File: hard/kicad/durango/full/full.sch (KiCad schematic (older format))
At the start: 38 parts, among them J1 NANOLINK, J2 IOX8, J3 BIOX9, J4 BUZZER, Q1 BC547, Q2 BC547, Q3 BC547, SW1 RESET, U1 65C02, U104 74HC257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

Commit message: adapting references to breadboard
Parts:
- U19: value 74HC00* -> 74HC00
- U20: value 74HC74* -> 74HC74
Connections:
- net A0: now also U20.12 (D); no longer U20.2 (D)
- net D0: now also U20.2 (D); no longer U20.12 (D)
- net GND: now also U28.1; no longer U28.2
- net IEN: now also U20.9 (Q); no longer U20.5 (Q)
- net ~DWE: now also U28.8; no longer U28.11
- net ~IEN: now also U20.8 (~Q); no longer U20.6 (~Q)
- net ~IOAQ: now also U20.11 (C); no longer U20.3 (C)
- net ~IOBQ: now also U20.3 (C); no longer U20.11 (C)
- net ~WE: now also U28.2, U28.9; no longer U28.1, U28.13
- net ~WE2: now also U28.12, U28.13; no longer U28.10, U28.9
- net ~WE3: now also U28.10, U28.11; no longer U28.12, U28.8
- net at D2.2 (A): now also U20.5 (Q); no longer U20.9 (Q)
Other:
- moved on the sheet: U20A, U20B, U28C, U28D
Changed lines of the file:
@@
 EESchema Schematic File Version 4
 LIBS:full-cache
-EELAYER 29 0
+EELAYER 30 0
 EELAYER END
 $Descr A4 11693 8268
@@
 P 3450 4200
 F 0 "U19" V 3404 4020 50  0000 R CNN
-F 1 "74HC00*" V 3495 4020 50  0000 R CNN
+F 1 "74HC00" V 3495 4020 50  0000 R CNN
 F 2 "Package_DIP:DIP-14_W7.62mm" H 3450 4200 50  0001 C CNN
 F 3 "http://www.ti.com/lit/gpn/sn74hct00" H 3450 4200 50  0001 C CNN
@@
 P 3750 4700
 F 0 "U19" H 3400 4500 50  0000 L CNN
-F 1 "74HC00*" H 3650 4500 50  0000 L CNN
+F 1 "74HC00" H 3650 4500 50  0000 L CNN
 F 2 "Package_DIP:DIP-14_W7.62mm" H 3750 4700 50  0001 C CNN
 F 3 "http://www.ti.com/lit/gpn/sn74hct00" H 3750 4700 50  0001 C CNN
@@
 L 74xx:74HC74 U20
 U 1 1 61846FEF
+P 9400 5800
+F 0 "U20" H 9400 6281 50  0000 C CNN
+F 1 "74HC74" H 9400 6190 50  0000 C CNN
+F 2 "Package_DIP:DIP-14_W7.62mm" H 9400 5800 50  0001 C CNN
+F 3 "74xx/74hc_hct74.pdf" H 9400 5800 50  0001 C CNN
+	1    9400 5800
+	1    0    0    -1
+$EndComp
+$Comp
+L 74xx:74HC74 U20
+U 2 1 6184A5B7
 P 8400 5800
 F 0 "U20" H 8400 6281 50  0000 C CNN
-F 1 "74HC74*" H 8400 6190 50  0000 C CNN
+F 1 "74HC74" H 8400 6190 50  0000 C CNN
 F 2 "Package_DIP:DIP-14_W7.62mm" H 8400 5800 50  0001 C CNN
 F 3 "74xx/74hc_hct74.pdf" H 8400 5800 50  0001 C CNN
-	1    8400 5800
-	1    0    0    -1
-$EndComp
-$Comp
-L 74xx:74HC74 U20
-U 2 1 6184A5B7
-P 9400 5800
-F 0 "U20" H 9400 6281 50  0000 C CNN
-F 1 "74HC74*" H 9400 6190 50  0000 C CNN
-F 2 "Package_DIP:DIP-14_W7.62mm" H 9400 5800 50  0001 C CNN
-F 3 "74xx/74hc_hct74.pdf" H 9400 5800 50  0001 C CNN
-	2    9400 5800
+	2    8400 5800
 	1    0    0    -1
 $EndComp
@@
 Wire Wire Line
 	9100 5800 9100 6400
-Wire Wire Line
-	9100 6400 7200 6400
 Text Label 9100 5700 2    50   ~ 0
 D0
@@
 U 1 1 60967ED5
 P 10500 4500
-F 0 "U28" V 10454 4688 50  0000 L CNN
-F 1 "74HC32" V 10545 4688 50  0000 L CNN
+F 0 "U28" V 10350 4100 50  0000 L CNN
+F 1 "74HC32" V 10450 4050 50  0000 L CNN
 F 2 "Package_DIP:DIP-14_W7.62mm" H 10500 4500 50  0001 C CNN
 F 3 "http://www.ti.com/lit/gpn/sn74LS32" H 10500 4500 50  0001 C CNN
 	1    10500 4500
-	0    -1   1    0
+	0    1    1    0
 $EndComp
 $Comp
@@
 L 74xx:74LS32 U28
 U 3 1 6096C7E5
+P 9400 3900
+F 0 "U28" V 9450 4300 50  0000 R CNN
+F 1 "74HC32" V 9350 4400 50  0000 R CNN
+F 2 "Package_DIP:DIP-14_W7.62mm" H 9400 3900 50  0001 C CNN
+F 3 "http://www.ti.com/lit/gpn/sn74LS32" H 9400 3900 50  0001 C CNN
+	3    9400 3900
+	0    1    -1   0
+$EndComp
+$Comp
+L 74xx:74LS32 U28
+U 4 1 6096F4C6
 P 9600 4800
-F 0 "U28" H 9650 5000 50  0000 R CNN
-F 1 "74HC32" H 9700 4600 50  0000 R CNN
+F 0 "U28" H 9700 4500 50  0000 R CNN
+F 1 "74HC32" H 9750 4600 50  0000 R CNN
 F 2 "Package_DIP:DIP-14_W7.62mm" H 9600 4800 50  0001 C CNN
 F 3 "http://www.ti.com/lit/gpn/sn74LS32" H 9600 4800 50  0001 C CNN
-	3    9600 4800
-	-1   0    0    -1
-$EndComp
-$Comp
-L 74xx:74LS32 U28
-U 4 1 6096F4C6
-P 9400 3900
-F 0 "U28" V 9446 3720 50  0000 R CNN
-F 1 "74HC32" V 9355 3720 50  0000 R CNN
-F 2 "Package_DIP:DIP-14_W7.62mm" H 9400 3900 50  0001 C CNN
-F 3 "http://www.ti.com/lit/gpn/sn74LS32" H 9400 3900 50  0001 C CNN
-	4    9400 3900
-	0    -1   -1   0
+	4    9600 4800
+	-1   0    0    1
 $EndComp
 Wire Wire Line
@@
 Wire Wire Line
 	9900 4700 9900 4900
-Connection ~ 9900 4900
 Wire Wire Line
 	10400 4200 9500 4200
@@
 ~RESET
 Wire Wire Line
+	7200 6400 9100 6400
+Wire Wire Line
 	2550 6200 3000 6200
 Wire Wire Line
@@
 	5850 950  5850 5100
 Wire Bus Line
+	10800 650  10800 1650
+Wire Bus Line
 	7450 950  7450 5050
 Wire Bus Line
-	10800 650  10800 1650
-Wire Bus Line
 	1650 5800 1650 6900
 Wire Bus Line
@@
 Wire Bus Line
 	4250 700  4250 6450
+Connection ~ 9900 4900
 $EndSCHEMATC

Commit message: fixed 74HC00 notation
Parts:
- U19: value 74HC00* -> 74HC00
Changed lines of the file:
@@
 EESchema Schematic File Version 4
 LIBS:full-cache
-EELAYER 30 0
+EELAYER 29 0
 EELAYER END
 $Descr A4 11693 8268
@@
 P 3800 5900
 F 0 "U19" V 3900 6300 50  0000 R CNN
-F 1 "74HC00*" V 3700 6450 50  0000 R CNN
+F 1 "74HC00" V 3700 6450 50  0000 R CNN
 F 2 "Package_DIP:DIP-14_W7.62mm" H 3800 5900 50  0001 C CNN
 F 3 "http://www.ti.com/lit/gpn/sn74hct00" H 3800 5900 50  0001 C CNN
@@
 Wire Wire Line
 	7200 6400 9100 6400
+Connection ~ 9900 4900
 Wire Wire Line
 	2550 6200 3000 6200
@@
 	5850 950  5850 5100
 Wire Bus Line
+	7450 950  7450 5050
+Wire Bus Line
 	10800 650  10800 1650
 Wire Bus Line
-	7450 950  7450 5050
-Wire Bus Line
 	1650 5800 1650 6900
 Wire Bus Line
@@
 Wire Bus Line
 	4250 700  4250 6450
-Connection ~ 9900 4900
 $EndSCHEMATC

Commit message: fixing VA lines in Durango-X
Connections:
- net VA5: no longer U104.5 (I0b)
- net VA6: no longer U104.14 (I0c)
- net VA7: no longer U104.2 (I0a)
- net VA8: no longer U105.11 (I0d)
- net VA12 renamed VA12*
- net VA13 renamed VA13*
- net VA14 renamed VA14*
- net VA15 renamed VA15*
- net VA16 renamed VA16*
- net VA17 renamed VA17*
- net VA18 renamed VA18*
- net VA19 renamed VA19*
- net VA4 renamed VA4*
- net VA9 renamed VA9*
- new net VA5*: U104.5 (I0b)
- new net VA6*: U104.14 (I0c)
- new net VA7*: U104.2 (I0a)
- new net VA8*: U105.11 (I0d)
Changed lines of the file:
@@
 	7600 4100 7800 4100
 Text Label 7600 1050 0    50   ~ 0
-VA7
+VA7*
 Text Label 7600 1350 0    50   ~ 0
-VA5
+VA5*
 Text Label 7600 1650 0    50   ~ 0
-VA6
+VA6*
 Text Label 7600 1950 0    50   ~ 0
-VA4
+VA4*
 Text Label 7600 3200 0    50   ~ 0
-VA14
+VA14*
 Text Label 7600 3500 0    50   ~ 0
-VA9
+VA9*
 Text Label 7600 3800 0    50   ~ 0
-VA13
+VA13*
 Text Label 7600 4100 0    50   ~ 0
-VA8
+VA8*
 Entry Wire Line
 	5850 950  5950 1050
@@
 	5950 3500 6150 3500
 Text Label 5950 1050 0    50   ~ 0
-VA18
+VA18*
 Text Label 5950 1350 0    50   ~ 0
-VA16
+VA16*
 Text Label 5950 1650 0    50   ~ 0
-VA17
+VA17*
 Text Label 5950 1950 0    50   ~ 0
-VA15
+VA15*
 Text Label 5950 3500 0    50   ~ 0
-VA19
+VA19*
 Wire Wire Line
 	6150 4100 6100 4100
@@
 	4300 4350 4500 4350
 Text Label 4300 3450 0    50   ~ 0
-VA14
+VA14*
 Text Label 4300 3750 0    50   ~ 0
-VA12
+VA12*
 Text Label 4300 4050 0    50   ~ 0
-VA13
+VA13*
 Text Label 4300 4350 0    50   ~ 0
-VA9
+VA9*
 $Comp
 L 74xx:74LS257 U204

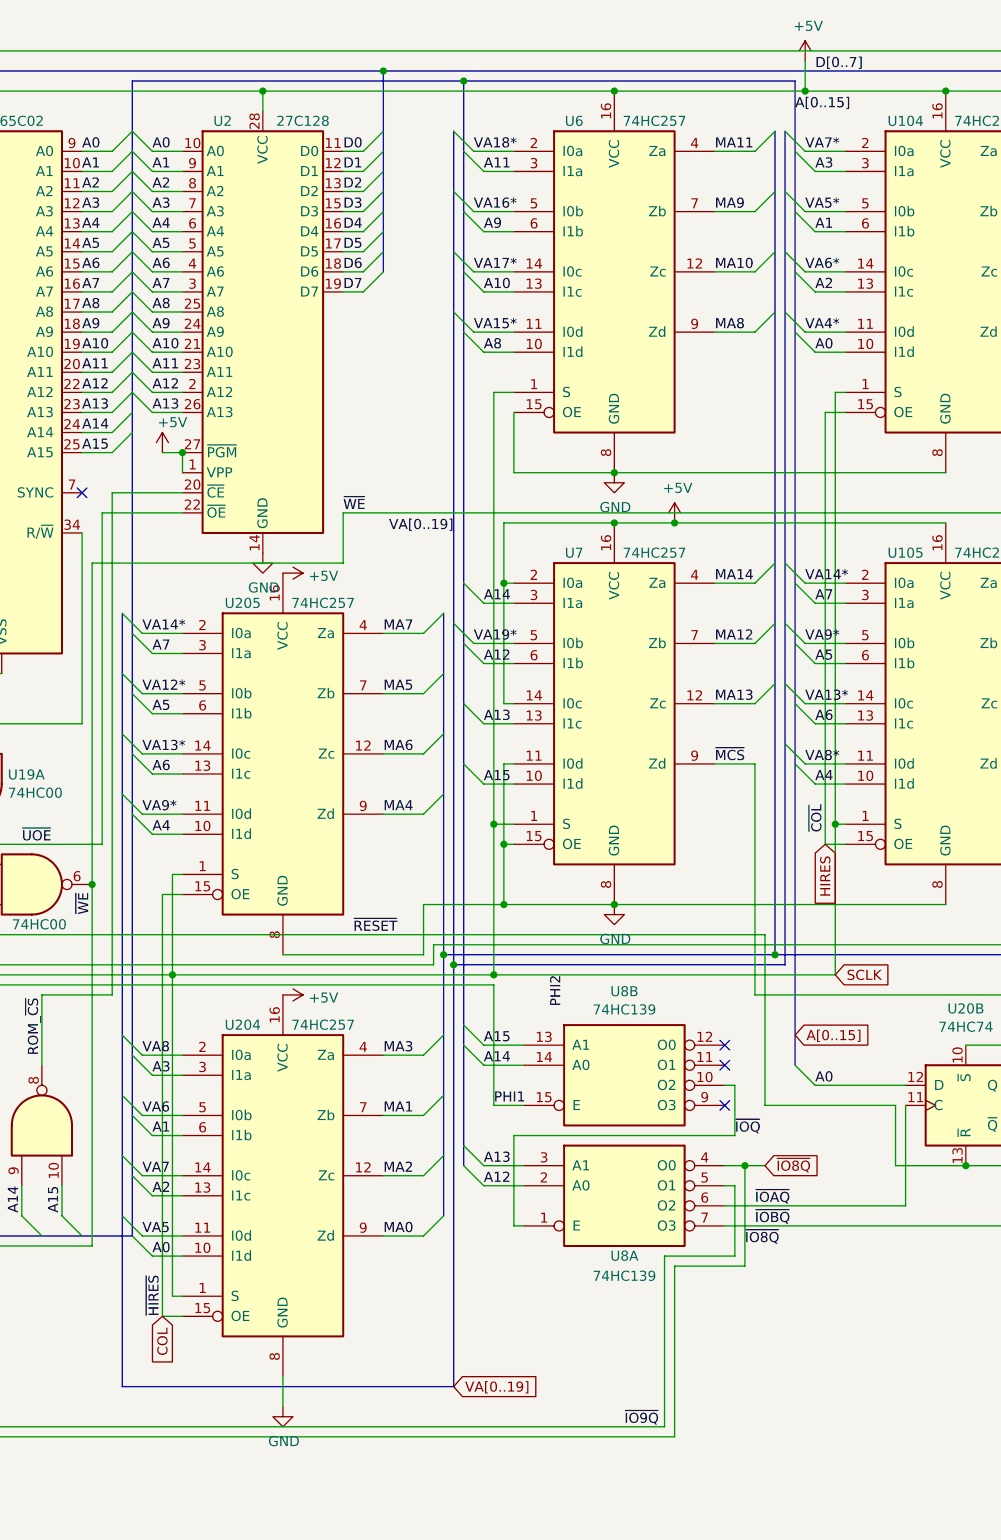
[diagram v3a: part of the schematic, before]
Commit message: severe fixes in Durango-X MUX
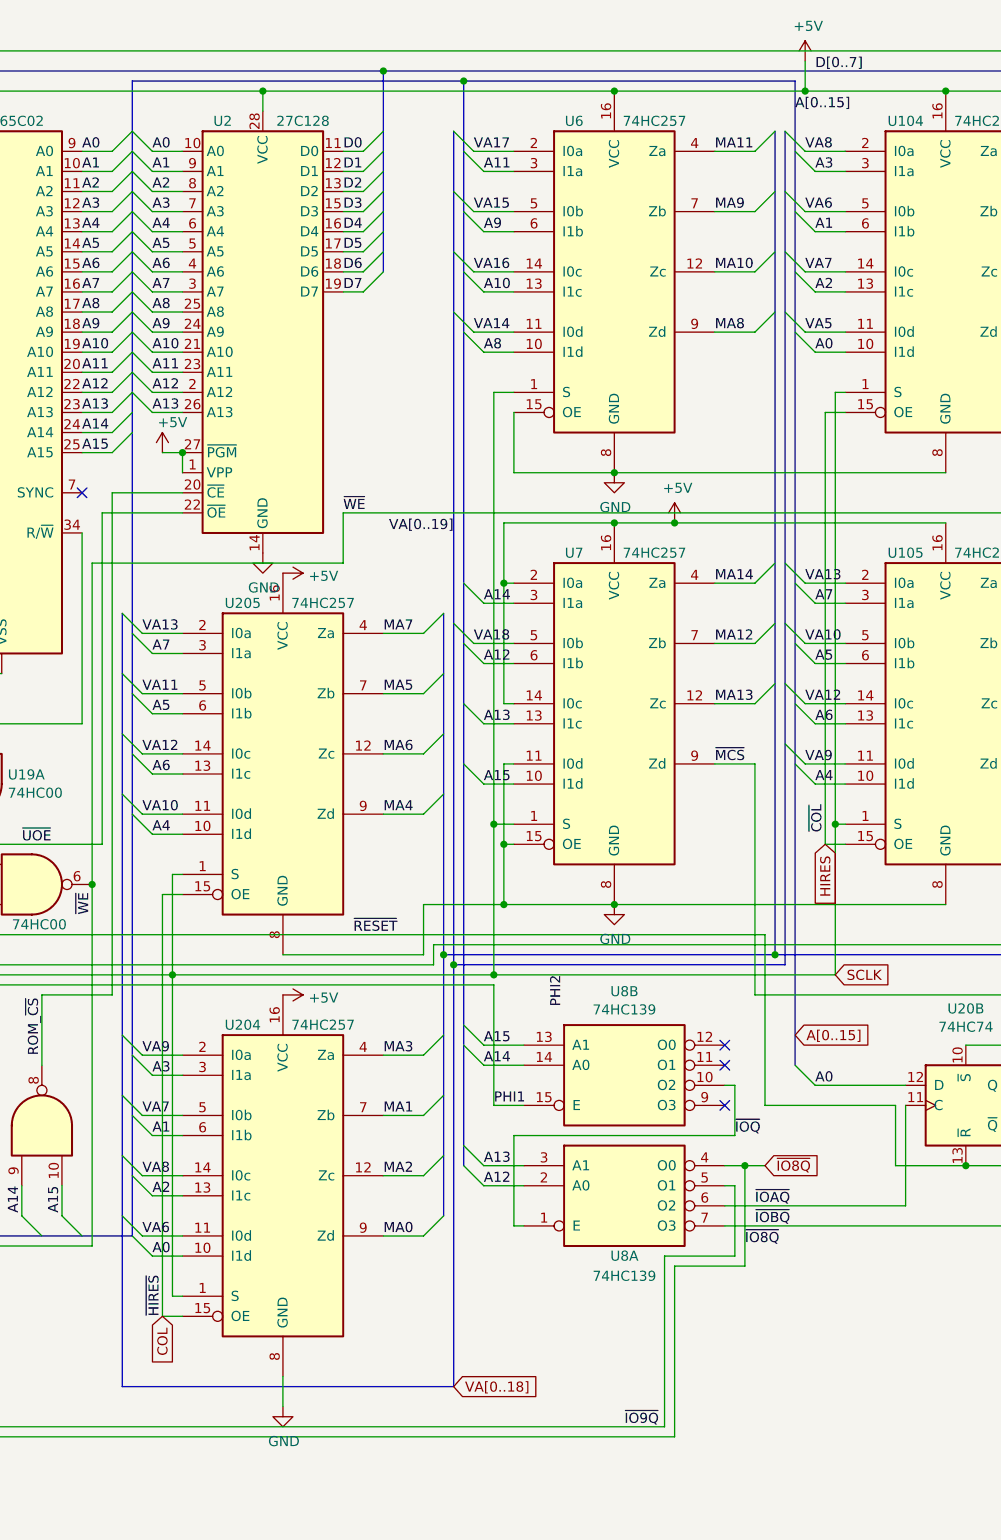
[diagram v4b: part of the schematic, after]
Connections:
- net VA4* is gone; now on net VA5: U104.11 (I0d)
- net VA5* is gone; now on net VA6: U104.5 (I0b)
- net VA6* is gone; now on net VA7: U104.14 (I0c)
- net VA7* is gone; now on net VA8: U104.2 (I0a)
- net VA5: no longer U204.11 (I0d)
- net VA6: now also U204.11 (I0d); no longer U204.5 (I0b)
- net VA7: now also U204.5 (I0b); no longer U204.14 (I0c)
- net VA8: now also U204.14 (I0c); no longer U204.2 (I0a)
- net VA12* renamed VA11
- net VA13* renamed VA12
- net VA14* renamed VA13
- net VA15* renamed VA14
- net VA16* renamed VA15
- net VA17* renamed VA16
- net VA18* renamed VA17
- net VA19* renamed VA18
- net VA8* renamed VA9
- net VA9: now also U204.2 (I0a)
- net VA9* renamed VA10
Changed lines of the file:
@@
 	7600 4100 7800 4100
 Text Label 7600 1050 0    50   ~ 0
-VA7*
+VA8
 Text Label 7600 1350 0    50   ~ 0
-VA5*
+VA6
 Text Label 7600 1650 0    50   ~ 0
-VA6*
+VA7
 Text Label 7600 1950 0    50   ~ 0
-VA4*
+VA5
 Text Label 7600 3200 0    50   ~ 0
-VA14*
+VA13
 Text Label 7600 3500 0    50   ~ 0
-VA9*
+VA10
 Text Label 7600 3800 0    50   ~ 0
-VA13*
+VA12
 Text Label 7600 4100 0    50   ~ 0
-VA8*
+VA9
 Entry Wire Line
 	5850 950  5950 1050
@@
 	5950 3500 6150 3500
 Text Label 5950 1050 0    50   ~ 0
-VA18*
+VA17
 Text Label 5950 1350 0    50   ~ 0
-VA16*
+VA15
 Text Label 5950 1650 0    50   ~ 0
-VA17*
+VA16
 Text Label 5950 1950 0    50   ~ 0
-VA15*
+VA14
 Text Label 5950 3500 0    50   ~ 0
-VA19*
+VA18
 Wire Wire Line
 	6150 4100 6100 4100
@@
 $EndSheet
 Text GLabel 5850 7200 2    50   Input ~ 0
-VA[0..19]
+VA[0..18]
 Text GLabel 2800 650  0    50   Input ~ 0
 D[0..7]
@@
 	4300 4350 4500 4350
 Text Label 4300 3450 0    50   ~ 0
-VA14*
+VA13
 Text Label 4300 3750 0    50   ~ 0
-VA12*
+VA11
 Text Label 4300 4050 0    50   ~ 0
-VA13*
+VA12
 Text Label 4300 4350 0    50   ~ 0
-VA9*
+VA10
 $Comp
 L 74xx:74LS257 U204
@@
 	4300 6450 4500 6450
 Text Label 4300 5550 0    50   ~ 0
+VA9
+Text Label 4300 5850 0    50   ~ 0
+VA7
+Text Label 4300 6150 0    50   ~ 0
 VA8
-Text Label 4300 5850 0    50   ~ 0
+Text Label 4300 6450 0    50   ~ 0
 VA6
-Text Label 4300 6150 0    50   ~ 0
-VA7
-Text Label 4300 6450 0    50   ~ 0
-VA5
 Wire Wire Line
 	4450 6750 4500 6750

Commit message: added IO circuitry
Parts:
- removed J3: BIOX9, Connector_PinHeader_2.54mm:PinHeader_2x12_P2.54mm_Vertical, symbol Connector_Generic:Conn_02x12_Odd_Even
- added J3: IOX9, Connector_PinHeader_2.54mm:PinHeader_2x08_P2.54mm_Vertical, symbol Connector_Generic:Conn_02x08_Odd_Even
- added U32, U33: 74HC245, symbol 74xx:74HC245
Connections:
- net +5V: now also J3.1 (Pin_1), U32.20 (VCC), U33.20 (VCC)
- net A0: no longer J2.3 (Pin_3)
- net A1: no longer J2.5 (Pin_5)
- net A2: no longer J2.7 (Pin_7)
- net A3: no longer J2.9 (Pin_9)
- net D0: now also U32.18 (B0), U33.18 (B0); no longer J2.2 (Pin_2)
- net D1: now also U32.17 (B1), U33.17 (B1); no longer J2.4 (Pin_4)
- net D2: now also U32.16 (B2), U33.16 (B2); no longer J2.6 (Pin_6)
- net D3: now also U32.15 (B3), U33.15 (B3); no longer J2.8 (Pin_8)
- net D4: now also U32.14 (B4), U33.14 (B4); no longer J2.10 (Pin_10)
- net D5: now also U32.13 (B5), U33.13 (B5); no longer J2.12 (Pin_12)
- net D6: now also U32.12 (B6), U33.12 (B6); no longer J2.14 (Pin_14)
- net D7: now also U32.11 (B7), U33.11 (B7); no longer J2.16 (Pin_16)
- net GND: now also J3.15 (Pin_15), U32.10 (GND), U33.10 (GND)
- net R~W: now also U32.1 (A->B), U33.1 (A->B)
- net ~IO8Q: now also J2.13 (Pin_13), U32.19 (CE); no longer J2.11 (Pin_11)
- net ~IO9Q: now also J3.13 (Pin_13), U33.19 (CE)
- net ~WE: no longer J2.13 (Pin_13)
- new net: J2.10 (Pin_10), U32.6 (A4)
- new net: J2.12 (Pin_12), U32.7 (A5)
- new net: J2.14 (Pin_14), U32.8 (A6)
- new net: J2.16 (Pin_16), U32.9 (A7)
- new net: J2.2 (Pin_2), U32.2 (A0)
- new net: J2.4 (Pin_4), U32.3 (A1)
- new net: J2.6 (Pin_6), U32.4 (A2)
- new net: J2.8 (Pin_8), U32.5 (A3)
- new net: J3.10 (Pin_10), U33.6 (A4)
- new net: J3.12 (Pin_12), U33.7 (A5)
- new net: J3.14 (Pin_14), U33.8 (A6)
- new net: J3.16 (Pin_16), U33.9 (A7)
- new net: J3.2 (Pin_2), U33.2 (A0)
- new net: J3.4 (Pin_4), U33.3 (A1)
- new net: J3.6 (Pin_6), U33.4 (A2)
- new net: J3.8 (Pin_8), U33.5 (A3)
- new net BA0: J2.3 (Pin_3), J3.3 (Pin_3)
- new net BA1: J2.5 (Pin_5), J3.5 (Pin_5)
- new net BA2: J2.7 (Pin_7), J3.7 (Pin_7)
- new net BA3: J2.9 (Pin_9), J3.9 (Pin_9)
- new net BA4: J2.11 (Pin_11), J3.11 (Pin_11)
- no-connect marks 20 -> 17
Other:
- moved on the sheet: J2, U19C, U8A, U8B

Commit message: hope I fixed all Durango-X VA bits
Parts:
- removed U17: 74HCT4020, Package_DIP:DIP-16_W7.62mm, symbol 4xxx:4020
- added U17: 74HCT4040, symbol 4xxx:4040
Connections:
- net +5V: now also U17.16 (VDD)
- net GND: now also U17.8 (VSS)
- net HZ250: now also U17.11 (Reset)
- net at U18.1: now also U17.15 (Q10)
- net at U18.2: now also U17.1 (Q11)
- new net VA4: U17.10 (CLK)
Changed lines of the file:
@@
 EESchema Schematic File Version 4
 LIBS:full-cache
-EELAYER 29 0
+EELAYER 30 0
 EELAYER END
 $Descr A4 11693 8268
@@
 $EndSheet
 Text GLabel 5850 7200 2    50   Input ~ 0
-VA[0..18]
+VA[2..18]
 Text GLabel 2800 650  0    50   Input ~ 0
 D[0..7]
@@
 Wire Wire Line
 	2900 2050 3000 2050
-$Comp
-L 4xxx:4020 U17
-U 1 1 60AC5D57
-P 1900 3750
-F 0 "U17" H 2050 4400 50  0000 C CNN
-F 1 "74HCT4020" H 1650 4400 50  0000 C CNN
-F 2 "Package_DIP:DIP-16_W7.62mm" H 1900 3750 50  0001 C CNN
-F 3 "http://www.intersil.com/content/dam/Intersil/documents/cd40/cd4020bms-24bms-40bms.pdf" H 1900 3750 50  0001 C CNN
-	1    1900 3750
-	-1   0    0    -1
-$EndComp
-Wire Wire Line
-	2400 3250 2900 3250
-Wire Wire Line
-	2900 2050 2900 3250
-Connection ~ 2900 3250
-Wire Wire Line
-	2900 3250 2900 4800
 NoConn ~ 1400 3250
 NoConn ~ 1400 3350
@@
 NoConn ~ 1400 3950
 NoConn ~ 1400 4050
-NoConn ~ 1400 4350
 $Comp
 L power:GND #PWR0125
 U 1 1 60C0180B
-P 1900 4650
-F 0 "#PWR0125" H 1900 4400 50  0001 C CNN
-F 1 "GND" H 1905 4477 50  0000 C CNN
-F 2 "" H 1900 4650 50  0001 C CNN
-F 3 "" H 1900 4650 50  0001 C CNN
-	1    1900 4650
+P 1900 4550
+F 0 "#PWR0125" H 1900 4300 50  0001 C CNN
+F 1 "GND" H 1905 4377 50  0000 C CNN
+F 2 "" H 1900 4550 50  0001 C CNN
+F 3 "" H 1900 4550 50  0001 C CNN
+	1    1900 4550
 	1    0    0    -1
 $EndComp
@@
 L power:+5V #PWR0126
 U 1 1 60C01E93
-P 1900 2950
-F 0 "#PWR0126" H 1900 2800 50  0001 C CNN
-F 1 "+5V" H 1800 3050 50  0000 C CNN
-F 2 "" H 1900 2950 50  0001 C CNN
-F 3 "" H 1900 2950 50  0001 C CNN
-	1    1900 2950
+P 1900 2850
+F 0 "#PWR0126" H 1900 2700 50  0001 C CNN
+F 1 "+5V" H 1800 2950 50  0000 C CNN
+F 2 "" H 1900 2850 50  0001 C CNN
+F 3 "" H 1900 2850 50  0001 C CNN
+	1    1900 2850
 	1    0    0    -1
 $EndComp
@@
 Text Label 2950 4500 0    50   ~ 0
 PHI1
-Wire Wire Line
-	4100 2850 4100 4500
 Wire Wire Line
 	9150 2650 9150 5250
@@
 Wire Wire Line
 	3100 7500 3500 7500
+Connection ~ 3500 7500
+Wire Wire Line
+	3500 7500 3500 7650
+$Comp
+L 4xxx:4040 U17
+U 1 1 6125842B
+P 1900 3650
+F 0 "U17" H 2300 4400 50  0000 C CNN
+F 1 "74HCT4040" H 2300 4300 50  0000 C CNN
+F 2 "" H 1900 3650 50  0001 C CNN
+F 3 "http://www.intersil.com/content/dam/Intersil/documents/cd40/cd4020bms-24bms-40bms.pdf" H 1900 3650 50  0001 C CNN
+	1    1900 3650
+	-1   0    0    -1
+$EndComp
+NoConn ~ 1400 3150
+Wire Wire Line
+	2900 2050 2900 4800
+Entry Wire Line
+	4100 3750 4200 3850
+Wire Wire Line
+	4100 3750 2450 3750
+Text Label 3800 3750 0    50   ~ 0
+VA4
+Wire Wire Line
+	2450 3150 2450 3750
+Wire Wire Line
+	2450 3150 2400 3150
 Wire Wire Line
 	10600 1050 10850 1050
@@
 	850  7600 3100 7600
 Wire Bus Line
-	4200 3350 4200 7200
-Wire Bus Line
 	7500 950  7500 5100
 Wire Bus Line
@@
 	5500 650  5500 1650
 Wire Bus Line
+	4200 3350 4200 7200
+Wire Bus Line
 	750  5550 2800 5550
 Wire Bus Line
@@
 Wire Bus Line
 	4250 700  4250 7300
-Connection ~ 3500 7500
-Wire Wire Line
-	3500 7500 3500 7650
+Wire Wire Line
+	4100 2850 4100 4500
 $EndSCHEMATC
